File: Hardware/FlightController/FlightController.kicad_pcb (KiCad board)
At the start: 2 copper layers, 30 parts, among them U1 STM32F405RGT6, U2 STM32H753VITx, U3 LMR54410DBVR, Y1 16MHz

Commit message: Add ICM-42670-P symbol and schematic
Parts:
- added C18: 10nF, Capacitor_SMD:C_0603_1608Metric, F.Cu at (162.7, 106.2)
- added C19: 0.1uF, Capacitor_SMD:C_0603_1608Metric, F.Cu at (167.3, 102.2)
- added C20: 2.2uF, Capacitor_SMD:C_0603_1608Metric, F.Cu at (162.7, 108.7)
- added R8: 2.2k, Resistor_SMD:R_0603_1608Metric, F.Cu at (160.7, 93.7)
- added R9: 2.2k, Resistor_SMD:R_0603_1608Metric, F.Cu at (156.7, 88.7)
- added U4: ICM-42670-P, Package_LGA:LGA-14_3x2.5mm_P0.5mm_LayoutBorder3x4y, F.Cu at (163.0, 103.0)
- R7: value 1.5k -> 1k
- moved R1 70.0 mm to (142.2, 111.7)
- moved C4 67.8 mm to (142.2, 114.2)
- moved C1 65.9 mm to (142.2, 109.2)
- moved D1 61.8 mm to (142.3, 106.7)
- moved R2 59.5 mm to (146.2, 109.2)
- moved C3 57.8 mm to (150.3, 104.7)
- moved R7 55.4 mm to (146.3, 106.6)
- moved C2 53.2 mm to (151.4, 102.2)
- moved C5 53.2 mm to (147.4, 102.2)
- moved C12 40.9 mm to (142.2, 96.1)
- moved C16 40.4 mm to (158.3, 96.2)
- moved C17 38.8 mm to (164.7, 91.7)
- moved C13 38.6 mm to (164.7, 89.2)
- moved R6 38.5 mm to (146.2, 96.1)
- moved C11 38.2 mm to (156.7, 93.7)
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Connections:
- net +3V3 renamed ACCEL_VDDIO
- net CAN_RX renamed S_CAN_RX
- net CAN_TX renamed S_CAN_TX
- U1 pad 29: S_USART3_TX -> S_I2C2_SCL
- U1 pad 30: S_USART3_RX -> S_I2C2_SDA
- U1 pad 51: unconnected-(U1-Pad51) -> S_USART3_TX
- U1 pad 52: unconnected-(U1-Pad52) -> S_USART3_RX

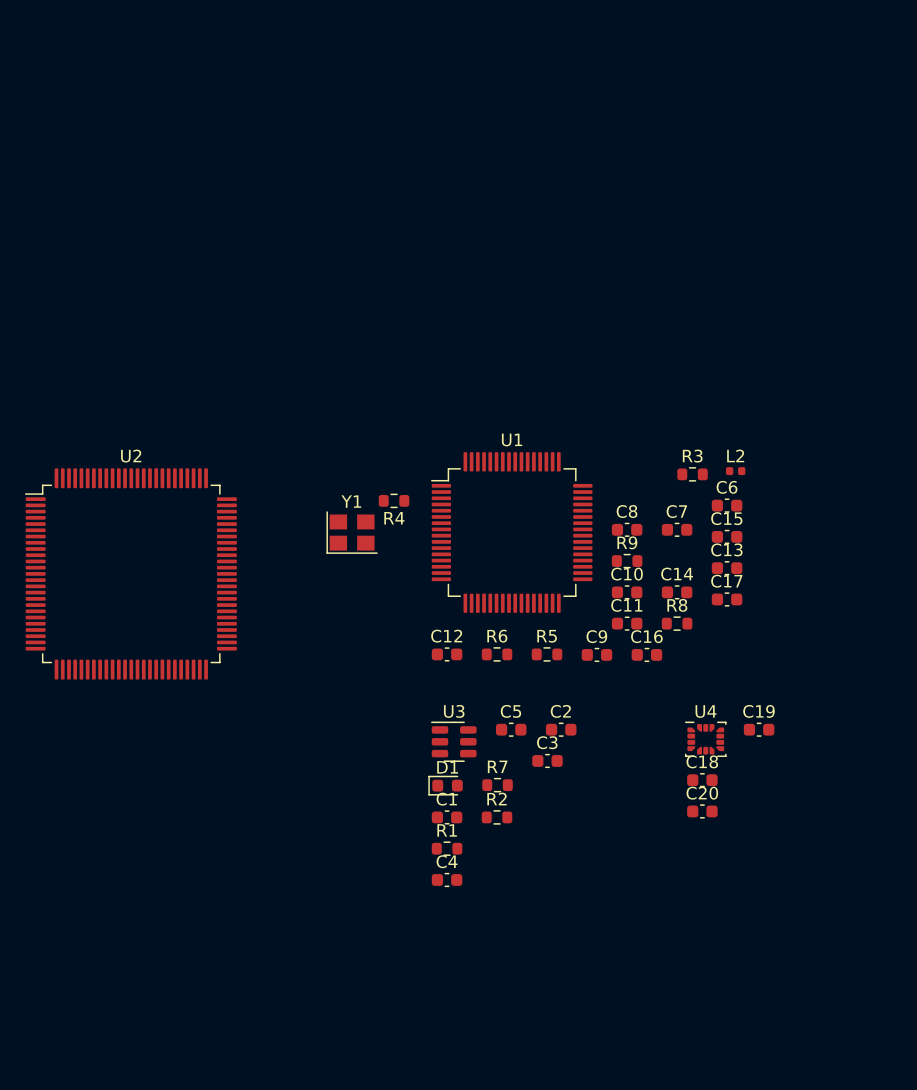
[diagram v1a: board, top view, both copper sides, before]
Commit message: Round out basic schematic and add preliminary board layout
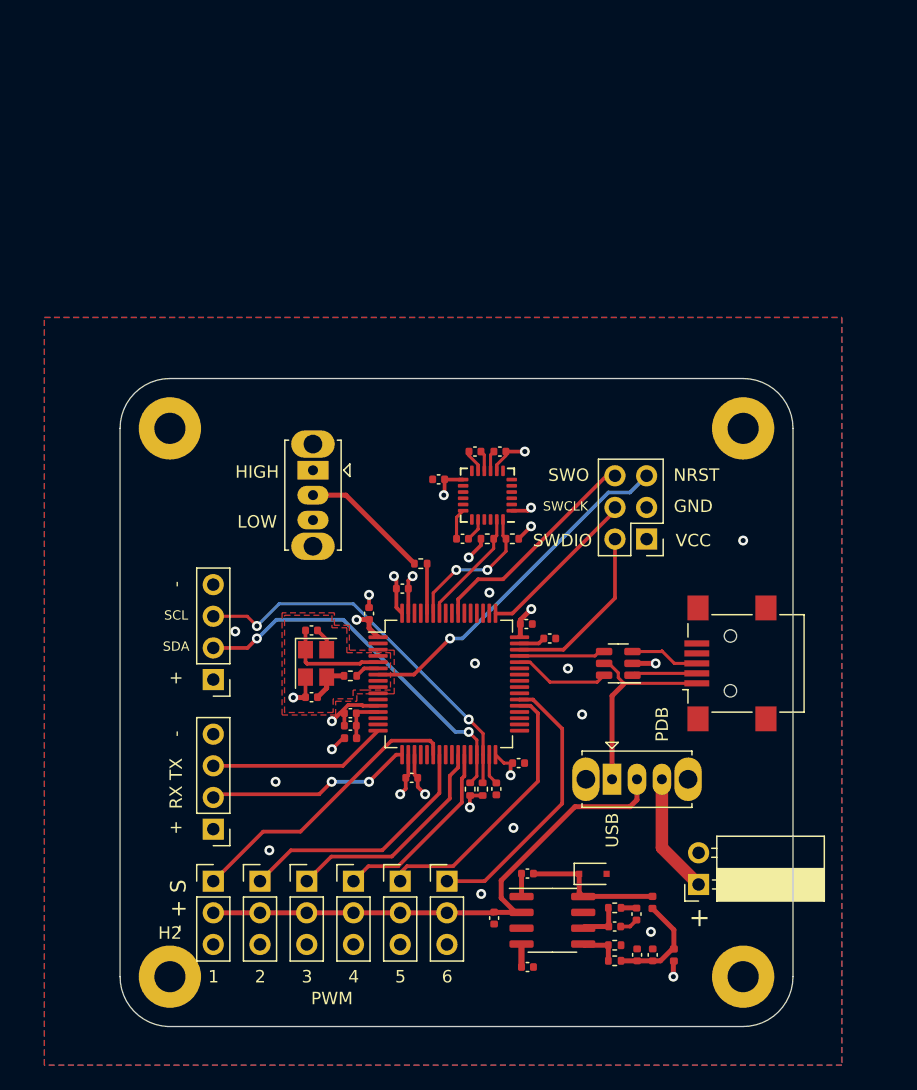
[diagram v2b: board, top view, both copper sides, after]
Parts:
- removed C19: 0.1uF, Capacitor_SMD:C_0603_1608Metric
- removed C20: 2.2uF, Capacitor_SMD:C_0603_1608Metric
- added C21: 0.1uF, Capacitor_SMD:C_0402_1005Metric, F.Cu at (146.5, 79.9)
- added C22: 0.1uF, Capacitor_SMD:C_0402_1005Metric, F.Cu at (141.6, 82.1)
- added C23: 0.1uF, Capacitor_SMD:C_0402_1005Metric, F.Cu at (144.5, 79.9)
- added C24: 2.2uF, Capacitor_SMD:C_0402_1005Metric, F.Cu at (143.5, 86.9)
- added F1: 750mA, Fuse:Fuse_0402_1005Metric, F.Cu at (160.4, 120.3)
- added H1: MountingHole_Pad, MountingHole:MountingHole_2.5mm_Pad, F.Cu at (166.0, 122.0)
- added H1: MountingHole_Pad, MountingHole:MountingHole_2.5mm_Pad, F.Cu at (120.0, 78.0)
- added H2: MountingHole_Pad, MountingHole:MountingHole_2.5mm_Pad, F.Cu at (120.0, 122.0)
- added H3: MountingHole_Pad, MountingHole:MountingHole_2.5mm_Pad, F.Cu at (166.0, 78.0)
- added J1: Conn_01x02, Connector_PinSocket_2.54mm:PinSocket_1x02_P2.54mm_Horizontal, F.Cu at (162.4, 114.6)
- added J10: Conn_01x03, Connector_PinHeader_2.54mm:PinHeader_1x03_P2.54mm_Vertical, F.Cu at (142.2, 114.3)
- added J11: Conn_01x04, Connector_PinHeader_2.54mm:PinHeader_1x04_P2.54mm_Vertical, F.Cu at (123.5, 98.2)
- added J2: USB_B_Mini, Connector_USB:USB_Mini-B_Lumberg_2486_01_Horizontal, F.Cu at (165.0, 96.9)
- added J3: Conn_02x03_Odd_Even, Connector_PinHeader_2.54mm:PinHeader_2x03_P2.54mm_Vertical, F.Cu at (158.3, 86.9)
- added J4: Conn_01x04, Connector_PinHeader_2.54mm:PinHeader_1x04_P2.54mm_Vertical, F.Cu at (123.5, 110.2)
- added J5: Conn_01x03, Connector_PinHeader_2.54mm:PinHeader_1x03_P2.54mm_Vertical, F.Cu at (123.5, 114.3)
- added J6: Conn_01x03, Connector_PinHeader_2.54mm:PinHeader_1x03_P2.54mm_Vertical, F.Cu at (127.2, 114.3)
- added J7: Conn_01x03, Connector_PinHeader_2.54mm:PinHeader_1x03_P2.54mm_Vertical, F.Cu at (131.0, 114.3)
- added J8: Conn_01x03, Connector_PinHeader_2.54mm:PinHeader_1x03_P2.54mm_Vertical, F.Cu at (134.7, 114.3)
- added J9: Conn_01x03, Connector_PinHeader_2.54mm:PinHeader_1x03_P2.54mm_Vertical, F.Cu at (138.5, 114.3)
- added L1: 6.8uH, Inductor_SMD:L_0402_1005Metric, F.Cu at (158.7, 116.0)
- added SW1: SW_SPDT, Button_Switch_THT:SW_Slide_1P2T_CK_OS102011MS2Q, F.Cu at (131.5, 81.4)
- added SW2: SW_SPDT, Button_Switch_THT:SW_Slide_1P2T_CK_OS102011MS2Q, F.Cu at (155.5, 106.2)
- C1: value 4.7uF -> 10uF; footprint Capacitor_SMD:C_0603_1608Metric -> Capacitor_SMD:C_0402_1005Metric
- C10, C11, C12, C13, C14, C16, C17, C6, C7, C8, C9: footprint Capacitor_SMD:C_0603_1608Metric -> Capacitor_SMD:C_0402_1005Metric
- C15: value 100nF -> 22uF; footprint Capacitor_SMD:C_0603_1608Metric -> Capacitor_SMD:C_0402_1005Metric
- C18: value 10nF -> 22uF; footprint Capacitor_SMD:C_0603_1608Metric -> Capacitor_SMD:C_0402_1005Metric
- C2: value 100nF -> 10pF; footprint Capacitor_SMD:C_0603_1608Metric -> Capacitor_SMD:C_0402_1005Metric
- C3: value 100nF -> 3nF; footprint Capacitor_SMD:C_0603_1608Metric -> Capacitor_SMD:C_0402_1005Metric
- C4: value 10uF -> 8.2nF; footprint Capacitor_SMD:C_0603_1608Metric -> Capacitor_SMD:C_0402_1005Metric
- C5: value 10uF -> 100nF; footprint Capacitor_SMD:C_0603_1608Metric -> Capacitor_SMD:C_0402_1005Metric
- D1: value RED -> PMEG4010EJ; footprint LED_SMD:LED_0603_1608Metric -> Diode_SMD:D_SOD-323F
- R1: value 69.8k -> 11.5k; footprint Resistor_SMD:R_0603_1608Metric -> Resistor_SMD:R_0402_1005Metric
- R2: value 22.1k -> 10.2k; footprint Resistor_SMD:R_0603_1608Metric -> Resistor_SMD:R_0402_1005Metric
- R3, R4: footprint Resistor_SMD:R_0603_1608Metric -> Resistor_SMD:R_0402_1005Metric
- R5, R6, R8, R9: value 2.2k -> 4.7k; footprint Resistor_SMD:R_0603_1608Metric -> Resistor_SMD:R_0402_1005Metric
- R7: value 1k -> 3.24k; footprint Resistor_SMD:R_0603_1608Metric -> Resistor_SMD:R_0402_1005Metric
- U2: value STM32H753VITx -> MPU-6050; footprint Package_QFP:LQFP-100_14x14mm_P0.5mm -> Sensor_Motion:InvenSense_QFN-24_4x4mm_P0.5mm
- U3: value LMR54410DBVR -> TPS54331DR; footprint Package_TO_SOT_SMD:SOT-23-6 -> Package_SO:SOIC-8_3.9x4.9mm_P1.27mm
- U4: value ICM-42670-P -> USBLC6-2SC6; footprint Package_LGA:LGA-14_3x2.5mm_P0.5mm_LayoutBorder3x4y -> Package_TO_SOT_SMD:SOT-23-6
- moved L2 37.6 mm to (134.5, 102.9)
- moved C6 34.8 mm to (131.4, 94.2)
- moved C15 34.3 mm to (157.5, 120.3), turned to 90 degrees
- moved C7 32.3 mm to (131.4, 99.6), turned to 180 degrees
- moved C17 31.9 mm to (134.5, 101.9), turned to 180 degrees
- moved U2 29.3 mm to (145.5, 83.4), turned to 180 degrees
- moved C16 24.3 mm to (134.5, 100.9), turned to 180 degrees
- moved R3 23.0 mm to (140.1, 88.9), turned to 180 degrees
- moved C14 22.0 mm to (138.7, 90.9)
- moved C8 21.8 mm to (136.0, 92.9), turned to 90 degrees
- moved R9 21.7 mm to (145.1, 107.0), turned to -90 degrees
- moved R8 21.3 mm to (144.1, 107.0), turned to -90 degrees
- moved C10 18.9 mm to (146.2, 106.9), turned to -90 degrees
- moved C9 17.8 mm to (139.4, 106.0), turned to 180 degrees
- moved C13 16.7 mm to (148.6, 93.7)
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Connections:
- C1 pad 1: +BATT -> +5V
- C11 pad 1: ACCEL_VDDIO -> +3V3
- C13 pad 1: ACCEL_VDDIO -> +3V3
- C14 pad 1: ACCEL_VDDIO -> +3V3
- C15 pad 1: ACCEL_VDDIO -> Net-(C15-Pad1)
- C18 pad 1: ACCEL_VDDIO -> Net-(C15-Pad1)
- C2 pad 1: +BATT -> Net-(C2-Pad1)
- C3 pad 2: Net-(C3-Pad2) -> GND
- C4 pad 1: ACCEL_VDDIO -> Net-(C4-Pad1)
- C5 pad 1: ACCEL_VDDIO -> Net-(C5-Pad1)
- C5 pad 2: GND -> Net-(C5-Pad2)
- C8 pad 1: ACCEL_VDDIO -> +3V3
- C9 pad 1: ACCEL_VDDIO -> +3V3
- D1 pad 1: Net-(D1-Pad1) -> Net-(C5-Pad2)
- D1 pad 2: ACCEL_VDDIO -> GND
- L2 pad 1: ACCEL_VDDIO -> +3V3
- R1 pad 1: ACCEL_VDDIO -> Net-(C2-Pad1)
- R1 pad 2: Net-(R1-Pad2) -> Net-(C3-Pad1)
- R2 pad 1: Net-(R1-Pad2) -> Net-(C15-Pad1)
- R2 pad 2: GND -> Net-(R2-Pad2)
- R5 pad 2: ACCEL_VDDIO -> +3V3
- R6 pad 2: ACCEL_VDDIO -> +3V3
- R7 pad 1: Net-(D1-Pad1) -> Net-(R2-Pad2)
- R8 pad 2: ACCEL_VDDIO -> +3V3
- R9 pad 2: ACCEL_VDDIO -> +3V3
- U1 pad 1: ACCEL_VDDIO -> +3V3
- U1 pad 19: ACCEL_VDDIO -> +3V3
- U1 pad 22: unconnected-(U1-Pad22) -> S_TIM3_CH1
- U1 pad 23: unconnected-(U1-Pad23) -> S_TIM3_CH2
- U1 pad 26: unconnected-(U1-Pad26) -> S_TIM3_CH3
- U1 pad 27: unconnected-(U1-Pad27) -> S_TIM3_CH4
- U1 pad 32: ACCEL_VDDIO -> +3V3
- U1 pad 37: unconnected-(U1-Pad37) -> S_TIM8_CH1
- U1 pad 38: unconnected-(U1-Pad38) -> S_TIM8_CH2
- U1 pad 48: ACCEL_VDDIO -> +3V3
- U1 pad 51: S_USART3_TX -> unconnected-(U1-Pad51)
- U1 pad 52: S_USART3_RX -> unconnected-(U1-Pad52)
- U1 pad 61: S_CAN_RX -> unconnected-(U1-Pad61)
- U1 pad 62: S_CAN_TX -> unconnected-(U1-Pad62)
- U1 pad 64: ACCEL_VDDIO -> +3V3
- U2 pad 1: unconnected-(U2-Pad1) -> GND
- U2 pad 10: unconnected-(U2-Pad10) -> Net-(C23-Pad2)
- U2 pad 11: unconnected-(U2-Pad11) -> GND
- U2 pad 13: unconnected-(U2-Pad13) -> +3V3
- U2 pad 18: unconnected-(U2-Pad18) -> GND
- U2 pad 20: unconnected-(U2-Pad20) -> Net-(C24-Pad1)
- U2 pad 23: unconnected-(U2-Pad23) -> S_I2C1_SCL
- U2 pad 24: unconnected-(U2-Pad24) -> S_I2C1_SDA
- U2 pad 8: unconnected-(U2-Pad8) -> +3V3
- U2 pad 9: unconnected-(U2-Pad9) -> GND
- U3 pad 1: Net-(C3-Pad2) -> Net-(C5-Pad1)
- U3 pad 2: GND -> +5V
- U3 pad 3: Net-(R1-Pad2) -> unconnected-(U3-Pad3)
- U3 pad 4: +BATT -> Net-(C4-Pad1)
- U3 pad 5: +BATT -> Net-(R2-Pad2)
- U3 pad 6: Net-(C3-Pad1) -> Net-(C2-Pad1)
- U4 pad 1: unconnected-(U4-Pad1) -> USB_CONN_DM
- U4 pad 2: unconnected-(U4-Pad2) -> GND
- U4 pad 3: unconnected-(U4-Pad3) -> USB_CONN_DP
- U4 pad 4: unconnected-(U4-Pad4) -> S_USB_DP
- U4 pad 5: ACCEL_VDDIO -> USB_5v
- U4 pad 6: GND -> S_USB_DM
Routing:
- net +5V: track 0.00 -> 43.5 mm
- net S_I2C2_SDA: track 0.00 -> 31.0 mm, vias 0 -> 2
- net S_I2C2_SCL: track 0.00 -> 29.7 mm, vias 0 -> 2
- net GND: track 0.00 -> 29.6 mm, vias 0 -> 18
- net +3V3: track 0.00 -> 28.9 mm, vias 0 -> 12
- net S_NRST: track 0.00 -> 28.2 mm, vias 0 -> 1
- net S_TIM3_CH1: track 0.00 -> 23.3 mm
- net S_TIM8_CH2: track 0.00 -> 22.2 mm
- net S_TIM8_CH1: track 0.00 -> 21.9 mm
- net S_TIM3_CH2: track 0.00 -> 20.4 mm
- net S_TIM3_CH3: track 0.00 -> 18.0 mm
- net S_SWO: track 0.00 -> 17.8 mm
- net S_USART2_RX: track 0.00 -> 16.6 mm, vias 0 -> 2
- net USB_5v: track 0.00 -> 16.4 mm
- net S_TIM3_CH4: track 0.00 -> 15.2 mm
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- added copper zone on In2.Cu, net +3V3
- added copper zone on B.Cu, net GND
- added copper zone on F.Cu, net GND
- added copper zone on In1.Cu, net GND
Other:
- board outline added: 54 x 52 mm
- copper layers 2 -> 4
- board text added: "+"
- board text added: "-"
- board text added: "- + S"
- board text added: "1"
- board text added: "2"
- board text added: "3"
- board text added: "4"
- board text added: "5"
- board text added: "6"
- board text added: "GND"
- board text added: "HIGH"
- board text added: "LOW"
- board text added: "NRST"
- board text added: "PDB"
- board text added: "PWM"
- board text added: "RX TX"
- board text added: "SCL"
- board text added: "SDA"
- board text added: "SWCLK"
- board text added: "SWDIO"
- board text added: "SWO"
- board text added: "USB"
- board text added: "VCC"

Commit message: Add and route SBUS inverter
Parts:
- added C19: 2.2uF, Capacitor_SMD:C_0402_1005Metric, F.Cu at (151.0, 77.5)
- added J12: Conn_01x03, Connector_PinHeader_2.54mm:PinHeader_1x03_P2.54mm_Vertical, F.Cu at (164.0, 83.7)
- added J13: Conn_01x02, Connector_PinHeader_2.54mm:PinHeader_1x02_P2.54mm_Vertical, F.Cu at (167.8, 86.2)
- added Q1: MMBT3904, Package_TO_SOT_SMD:SOT-23, F.Cu at (158.0, 88.8)
- added R10: 1k, Resistor_SMD:R_0402_1005Metric, F.Cu at (159.4, 91.2)
- added R11: 1k, Resistor_SMD:R_0402_1005Metric, F.Cu at (157.0, 86.0)
- added U5: MMC5603NJ, Package_BGA:WLP-4_0.83x0.83mm_P0.4mm, F.Cu at (151.5, 79.5)
- moved J3 4.89 mm to (158.8, 82.0)
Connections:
- U1 pad 42: unconnected-(U1-Pad42) -> SBUS_TX
- U1 pad 43: unconnected-(U1-Pad43) -> S_SBUS_RX
- U2 pad 6: unconnected-(U2-Pad6) -> AUX_SDA
- U2 pad 7: unconnected-(U2-Pad7) -> AUX_SCL
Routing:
- net SBUS_TX: track 0.00 -> 24.0 mm, vias 0 -> 1
- net S_SBUS_RX: track 0.00 -> 20.7 mm, vias 0 -> 1
- net AUX_SCL: track 0.00 -> 12.0 mm, vias 0 -> 2
- net /MCU/SBUS_RX_INV: track 0.00 -> 10.5 mm
- net SBUS_RX: track 0.00 -> 9.93 mm
- net +3V3: track 28.9 -> 38.3 mm
- net AUX_SDA: track 0.00 -> 5.30 mm
- net S_SWDIO: track 14.1 -> 19.2 mm
- net S_NRST: track 28.2 -> 33.2 mm
- net S_SWCLK: track 13.3 -> 18.2 mm
- net S_SWO: track 17.8 -> 22.5 mm
- net S_I2C2_SCL: track 29.7 -> 32.4 mm
- net GND: track 29.6 -> 31.3 mm, vias 18 -> 54
- net Net-(Q1-Pad1): track 0.00 -> 1.47 mm
- net S_I2C2_SDA: track 31.0 -> 32.4 mm
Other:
- board text added: "Boot Mode"
- board text added: "I2C"
- board text added: "INV"
- board text added: "UART"
- board text removed: "GND"
- board text removed: "NRST"
- board text removed: "SWCLK"
- board text removed: "SWDIO"
- board text removed: "SWO"
- board text removed: "VCC"

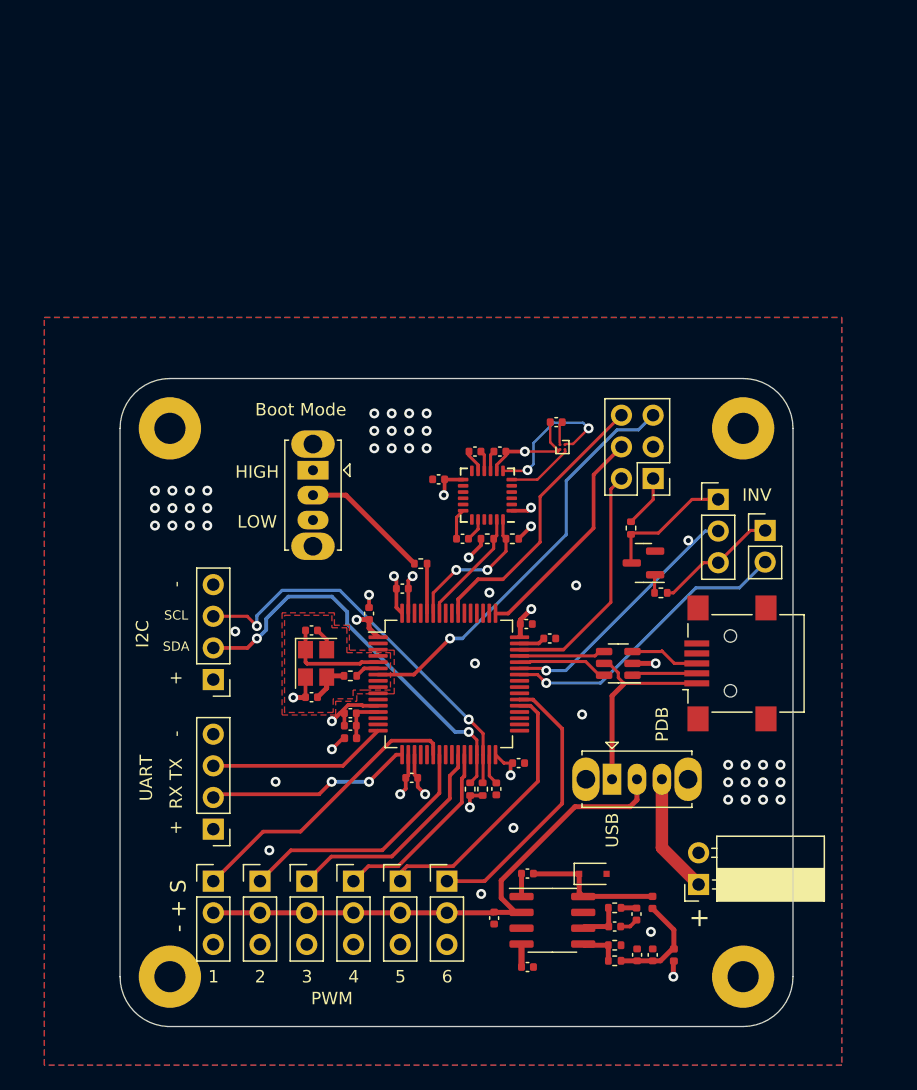
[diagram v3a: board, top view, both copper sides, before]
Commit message: Update footprints to be digikey compliant
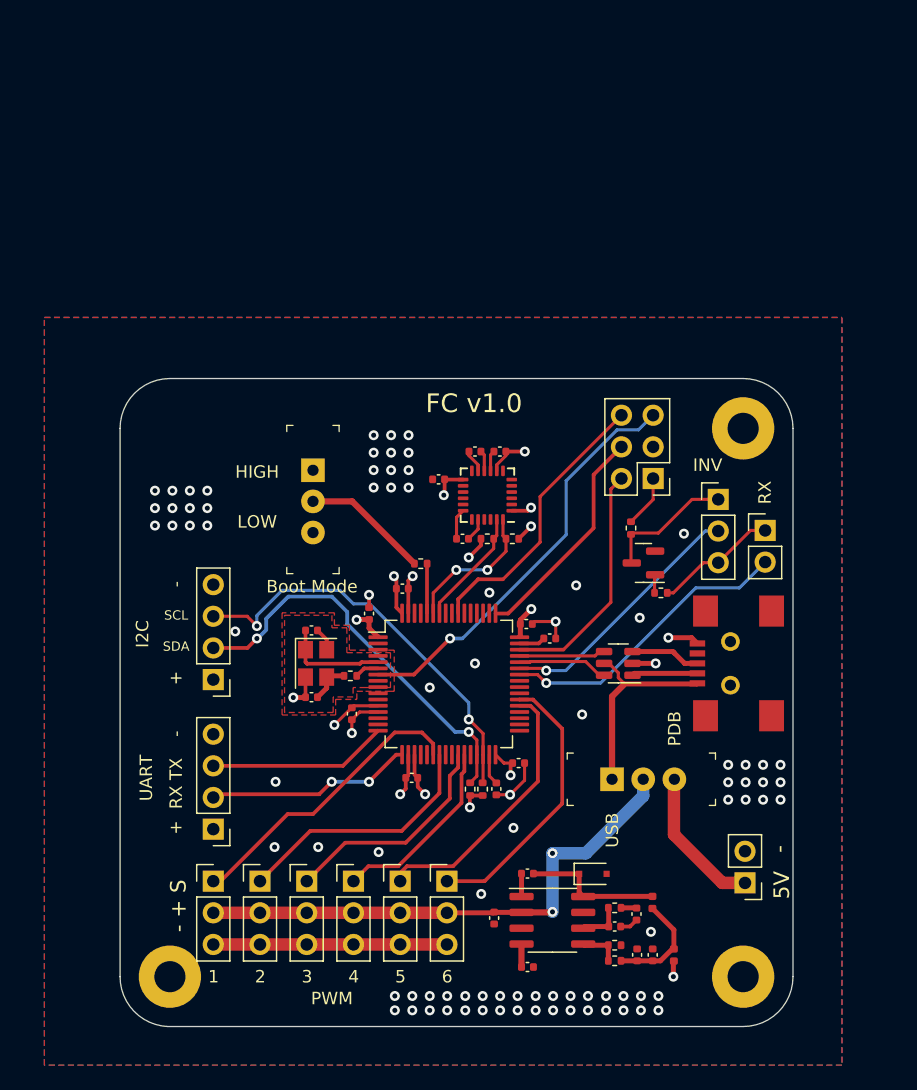
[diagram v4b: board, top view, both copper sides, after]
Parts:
- removed C17: 10nF, Capacitor_SMD:C_0402_1005Metric
- removed C19: 2.2uF, Capacitor_SMD:C_0402_1005Metric
- removed the H1 at (120.0, 78.0)
- removed L2: 39nH, Inductor_SMD:L_0402_1005Metric
- removed U5: MMC5603NJ, Package_BGA:WLP-4_0.83x0.83mm_P0.4mm
- C16: value 1uF -> 100nF
- J1: footprint Connector_PinSocket_2.54mm:PinSocket_1x02_P2.54mm_Horizontal -> Connector_PinHeader_2.54mm:PinHeader_1x02_P2.54mm_Vertical
- J2: footprint Connector_USB:USB_Mini-B_Lumberg_2486_01_Horizontal -> digikey-footprints:USB_Mini_B_Female_UX60-MB-5ST
- SW1, SW2: footprint Button_Switch_THT:SW_Slide_1P2T_CK_OS102011MS2Q -> digikey-footprints:Switch_Slide_11.6x4mm_EG1218
- moved J1 3.73 mm to (166.2, 114.5)
- moved C16 0.13 mm to (134.6, 100.9), turned to 90 degrees
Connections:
- C16 pad 1: +3.3VA -> +3V3
- U1 pad 13: +3.3VA -> +3V3
- U1 pad 21: unconnected-(U1-Pad21) -> S_SPI1_SCK
- U1 pad 56: unconnected-(U1-Pad56) -> S_SPI1_MISO
- U1 pad 57: unconnected-(U1-Pad57) -> S_SPI1_MOSI
- U2 pad 6: AUX_SDA -> unconnected-(U2-Pad6)
- U2 pad 7: AUX_SCL -> unconnected-(U2-Pad7)
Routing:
- net GND: track 31.3 -> 55.9 mm, vias 54 -> 93
- net AUX_SCL: track 12.0 -> 0.00 mm, vias 2 -> 0
- net AUX_SDA: track 5.30 -> 0.00 mm
- net +3.3VA: track 3.79 -> 0.00 mm
- net +3V3: track 38.3 -> 35.1 mm
- net PDB_REG_5v: track 9.66 -> 11.8 mm
- net S_I2C2_SDA: track 32.4 -> 33.2 mm
- net S_TIM3_CH1: track 23.3 -> 23.8 mm
- net +5V: vias 0 -> 2
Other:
- board text added: "5V"
- board text added: "FC v1.0"
- board text added: "RX"
